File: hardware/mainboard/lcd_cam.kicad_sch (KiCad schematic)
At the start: 57 parts, among them J5 Conn_01x02, J6 Conn_01x02, U18 MCP6566R, U19 ADP5070ACPZ, U20 CAT4106HV4, U22 74AHC1G08

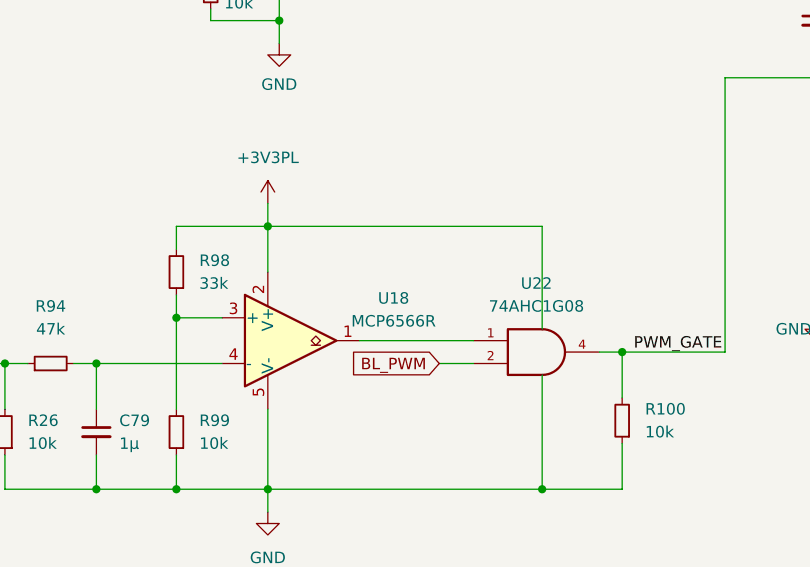
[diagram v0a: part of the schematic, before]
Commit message: Fix some ERC/DRC issues
Signed-off-by: gatecat <gatecat@ds0.me>
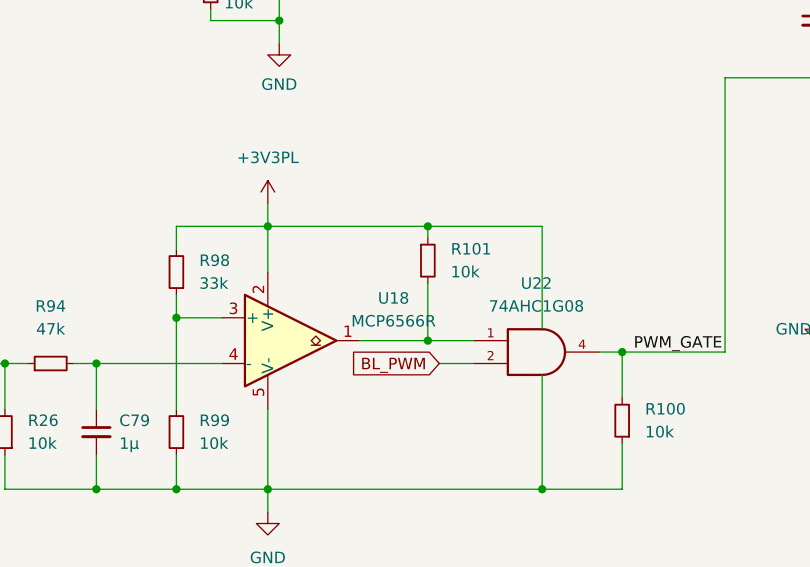
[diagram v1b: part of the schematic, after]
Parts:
- added R101: 10k, Resistor_SMD:R_0402_1005Metric, symbol Device:R_Small
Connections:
- net +3V3PL: now also R101.1
- net at U18.1, U22.1: now also R101.2
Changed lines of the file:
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@@
   (junction (at 311.15 69.85) (diameter 0) (color 0 0 0 0)
   )
+  (junction (at 151.13 251.46) (diameter 0) (color 0 0 0 0)
+  )
   (junction (at 194.31 210.82) (diameter 0) (color 0 0 0 0)
   )
@@
   (junction (at 311.15 46.99) (diameter 0) (color 0 0 0 0)
   )
+  (junction (at 151.13 238.76) (diameter 0) (color 0 0 0 0)
+  )
   (junction (at 311.15 158.75) (diameter 0) (color 0 0 0 0)
   )
@@
     (stroke (width 0) (type default) (color 0 0 0 0))
   )
+  (wire (pts (xy 151.13 245.11) (xy 151.13 251.46))
+    (stroke (width 0) (type default) (color 0 0 0 0))
+  )
   (wire (pts (xy 297.18 118.11) (xy 313.69 118.11))
     (stroke (width 0) (type default) (color 0 0 0 0))
@@
     (stroke (width 0) (type default) (color 0 0 0 0))
   )
-  (wire (pts (xy 133.35 238.76) (xy 163.83 238.76))
+  (wire (pts (xy 133.35 238.76) (xy 151.13 238.76))
     (stroke (width 0) (type default) (color 0 0 0 0))
   )
@@
     (stroke (width 0) (type default) (color 0 0 0 0))
   )
-  (wire (pts (xy 143.51 251.46) (xy 156.21 251.46))
+  (wire (pts (xy 143.51 251.46) (xy 151.13 251.46))
     (stroke (width 0) (type default) (color 0 0 0 0))
   )
@@
     (stroke (width 0) (type default) (color 0 0 0 0))
   )
+  (wire (pts (xy 151.13 251.46) (xy 156.21 251.46))
+    (stroke (width 0) (type default) (color 0 0 0 0))
+  )
   (wire (pts (xy 369.57 163.83) (xy 354.33 163.83))
     (stroke (width 0) (type default) (color 0 0 0 0))
@@
     (stroke (width 0) (type default) (color 0 0 0 0))
   )
+  (wire (pts (xy 151.13 238.76) (xy 163.83 238.76))
+    (stroke (width 0) (type default) (color 0 0 0 0))
+  )
   (wire (pts (xy 386.08 36.83) (xy 387.35 36.83))
     (stroke (width 0) (type default) (color 0 0 0 0))
@@
     (stroke (width 0) (type default) (color 0 0 0 0))
   )
+  (wire (pts (xy 151.13 238.76) (xy 151.13 240.03))
+    (stroke (width 0) (type default) (color 0 0 0 0))
+  )
   (wire (pts (xy 138.43 153.67) (xy 134.62 153.67))
     (stroke (width 0) (type default) (color 0 0 0 0))
@@
       (effects (font (size 1.27 1.27)) hide)
     )
+    (pin "1")
+    (pin "2")
+  )
+  (symbol (lib_id "Device:R_Small") (at 151.13 242.57 0) (unit 1)
+    (in_bom yes) (on_board yes) (fields_autoplaced)
+    (property "Reference" "R101" (id 0) (at 153.67 241.2999 0)
+      (effects (font (size 1.27 1.27)) (justify left))
+    )
+    (property "Value" "10k" (id 1) (at 153.67 243.8399 0)
+      (effects (font (size 1.27 1.27)) (justify left))
+    )
+    (property "Footprint" "Resistor_SMD:R_0402_1005Metric" (id 2) (at 151.13 242.57 0)
+      (effects (font (size 1.27 1.27)) hide)
+    )
+    (property "Datasheet" "~" (id 3) (at 151.13 242.57 0)
+      (effects (font (size 1.27 1.27)) hide)
+    )
